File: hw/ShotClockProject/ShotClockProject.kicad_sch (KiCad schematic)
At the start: 5 parts, among them SW5 SW_SPDT

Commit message: Renamed references
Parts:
- renumbered R8 to R1, R12 to R2, SW5 to SW1, TP8 to TP2
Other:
- note added: "SPDT here is the main power switch. The TP4056 should still be able to run, when the product is turned off (to charge Li-Po). The TP4056 gets powered directly from 5V Vbus (USB-c cable)."
- note removed: "SW5 is the main power switch. The TP4056 should still be able to run, when the product is turned off (to charge Li-Po). The TP4056 gets powered directly from 5V Vbus (USB-c cable)."
- moved on the sheet: R2, TP2
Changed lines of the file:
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@@
   (junction (at 59.69 49.53) (diameter 0) (color 0 0 0 0)
   )
-  (junction (at 149.86 48.26) (diameter 0) (color 0 0 0 0)
-  )
-  (junction (at 138.43 48.26) (diameter 0) (color 0 0 0 0)
+  (junction (at 149.86 50.8) (diameter 0) (color 0 0 0 0)
+  )
+  (junction (at 138.43 50.8) (diameter 0) (color 0 0 0 0)
   )
   (no_connect (at 81.28 46.99))
@@
     (stroke (width 0) (type default))
   )
-  (wire (pts (xy 138.43 48.26) (xy 139.7 48.26))
+  (wire (pts (xy 138.43 50.8) (xy 139.7 50.8))
     (stroke (width 0) (type default))
   )
@@
     (stroke (width 0) (type default))
   )
-  (wire (pts (xy 90.17 48.26) (xy 101.6 48.26))
+  (wire (pts (xy 90.17 50.8) (xy 90.17 52.07))
     (stroke (width 0) (type default))
   )
@@
     (stroke (width 0) (type default))
   )
-  (wire (pts (xy 125.73 48.26) (xy 138.43 48.26))
+  (wire (pts (xy 125.73 50.8) (xy 138.43 50.8))
     (stroke (width 0) (type default))
   )
@@
     (stroke (width 0) (type default))
   )
-  (wire (pts (xy 153.67 48.26) (xy 153.67 46.99))
+  (wire (pts (xy 153.67 50.8) (xy 153.67 49.53))
     (stroke (width 0) (type default))
   )
@@
     (stroke (width 0) (type default))
   )
-  (wire (pts (xy 147.32 48.26) (xy 149.86 48.26))
+  (wire (pts (xy 147.32 50.8) (xy 149.86 50.8))
     (stroke (width 0) (type default))
   )
@@
     (stroke (width 0) (type default))
   )
-  (wire (pts (xy 90.17 52.07) (xy 90.17 48.26))
-    (stroke (width 0) (type default))
-  )
   (wire (pts (xy 203.2 78.74) (xy 231.14 78.74))
     (stroke (width 0) (type default))
   )
-  (wire (pts (xy 149.86 48.26) (xy 153.67 48.26))
+  (wire (pts (xy 149.86 50.8) (xy 153.67 50.8))
+    (stroke (width 0) (type default))
+  )
+  (wire (pts (xy 101.6 50.8) (xy 90.17 50.8))
     (stroke (width 0) (type default))
   )
@@
     (effects (font (size 2.5 2.5) (color 255 0 0 1)) (justify left bottom))
   )
-  (text "SW5 is the main power switch.\nThe TP4056 should still be able to run, \nwhen the product is turned off (to charge Li-Po).\nThe TP4056 gets powered directly from 5V Vbus (USB-c cable)."
+  (text "SPDT here is the main power switch.\nThe TP4056 should still be able to run, \nwhen the product is turned off (to charge Li-Po).\nThe TP4056 gets powered directly from 5V Vbus (USB-c cable)."
     (at 46.99 83.82 0)
     (effects (font (size 1.27 1.27)) (justify left bottom))
@@
   (symbol (lib_id "Switch:SW_SPDT") (at 76.2 49.53 0) (unit 1)
     (in_bom yes) (on_board yes) (dnp no)
-    (property "Reference" "SW5" (at 73.66 52.07 0)
+    (property "Reference" "SW1" (at 73.66 52.07 0)
       (effects (font (size 1.27 1.27)))
     )
@@
       (project "ShotClockProject"
         (path "/5fd859aa-754d-49c2-9762-3f7ebe3bb64c"
-          (reference "SW5") (unit 1)
+          (reference "SW1") (unit 1)
         )
         (path "/5fd859aa-754d-49c2-9762-3f7ebe3bb64c/d53b1cd8-24cb-4dc0-9a02-0cd96c1f4291"
@@
   (symbol (lib_id "Device:R") (at 64.77 49.53 90) (unit 1)
     (in_bom yes) (on_board yes) (dnp no) (fields_autoplaced)
-    (property "Reference" "R8" (at 64.77 43.18 90)
+    (property "Reference" "R1" (at 64.77 43.18 90)
       (effects (font (size 1.27 1.27)))
     )
@@
       (project "ShotClockProject"
         (path "/5fd859aa-754d-49c2-9762-3f7ebe3bb64c"
-          (reference "R8") (unit 1)
-        )
-      )
-    )
-  )
-  (symbol (lib_id "Connector:TestPoint") (at 138.43 48.26 0) (mirror y) (unit 1)
+          (reference "R1") (unit 1)
+        )
+      )
+    )
+  )
+  (symbol (lib_id "Connector:TestPoint") (at 138.43 50.8 0) (mirror y) (unit 1)
     (in_bom yes) (on_board yes) (dnp no)
-    (property "Reference" "TP8" (at 137.16 43.18 0)
-      (effects (font (size 1.27 1.27)) (justify left))
-    )
-    (property "Value" "TestPoint" (at 137.16 45.72 0)
-      (effects (font (size 1.27 1.27)) (justify left))
-    )
-    (property "Footprint" "TestPoint:TestPoint_Pad_D2.5mm" (at 133.35 48.26 0)
-      (effects (font (size 1.27 1.27)) hide)
-    )
-    (property "Datasheet" "~" (at 133.35 48.26 0)
-      (effects (font (size 1.27 1.27)) hide)
-    )
-    (pin "1")
-    (instances
-      (project "ShotClockProject"
-        (path "/5fd859aa-754d-49c2-9762-3f7ebe3bb64c"
-          (reference "TP8") (unit 1)
+    (property "Reference" "TP2" (at 137.16 45.72 0)
+      (effects (font (size 1.27 1.27)) (justify left))
+    )
+    (property "Value" "TestPoint" (at 137.16 48.26 0)
+      (effects (font (size 1.27 1.27)) (justify left))
+    )
+    (property "Footprint" "TestPoint:TestPoint_Pad_D2.5mm" (at 133.35 50.8 0)
+      (effects (font (size 1.27 1.27)) hide)
+    )
+    (property "Datasheet" "~" (at 133.35 50.8 0)
+      (effects (font (size 1.27 1.27)) hide)
+    )
+    (pin "1")
+    (instances
+      (project "ShotClockProject"
+        (path "/5fd859aa-754d-49c2-9762-3f7ebe3bb64c"
+          (reference "TP2") (unit 1)
         )
         (path "/5fd859aa-754d-49c2-9762-3f7ebe3bb64c/17367eb9-0f4d-4017-b1ca-d50430410a5d"
@@
     )
   )
-  (symbol (lib_id "Device:R") (at 143.51 48.26 90) (unit 1)
+  (symbol (lib_id "Device:R") (at 143.51 50.8 90) (unit 1)
     (in_bom yes) (on_board yes) (dnp no) (fields_autoplaced)
-    (property "Reference" "R12" (at 143.51 41.91 90)
-      (effects (font (size 1.27 1.27)))
-    )
-    (property "Value" "0R" (at 143.51 44.45 90)
-      (effects (font (size 1.27 1.27)))
-    )
-    (property "Footprint" "Resistor_SMD:R_0603_1608Metric" (at 143.51 50.038 90)
-      (effects (font (size 1.27 1.27)) hide)
-    )
-    (property "Datasheet" "~" (at 143.51 48.26 0)
+    (property "Reference" "R2" (at 143.51 44.45 90)
+      (effects (font (size 1.27 1.27)))
+    )
+    (property "Value" "0R" (at 143.51 46.99 90)
+      (effects (font (size 1.27 1.27)))
+    )
+    (property "Footprint" "Resistor_SMD:R_0603_1608Metric" (at 143.51 52.578 90)
+      (effects (font (size 1.27 1.27)) hide)
+    )
+    (property "Datasheet" "~" (at 143.51 50.8 0)
       (effects (font (size 1.27 1.27)) hide)
     )
@@
       (project "ShotClockProject"
         (path "/5fd859aa-754d-49c2-9762-3f7ebe3bb64c"
-          (reference "R12") (unit 1)
-        )
-      )
-    )
-  )
-  (symbol (lib_id "power:PWR_FLAG") (at 149.86 48.26 180) (unit 1)
+          (reference "R2") (unit 1)
+        )
+      )
+    )
+  )
+  (symbol (lib_id "power:PWR_FLAG") (at 149.86 50.8 180) (unit 1)
     (in_bom yes) (on_board yes) (dnp no) (fields_autoplaced)
-    (property "Reference" "#FLG02" (at 149.86 50.165 0)
-      (effects (font (size 1.27 1.27)) hide)
-    )
-    (property "Value" "PWR_FLAG" (at 149.86 53.34 0)
-      (effects (font (size 1.27 1.27)))
-    )
-    (property "Footprint" "" (at 149.86 48.26 0)
-      (effects (font (size 1.27 1.27)) hide)
-    )
-    (property "Datasheet" "~" (at 149.86 48.26 0)
+    (property "Reference" "#FLG02" (at 149.86 52.705 0)
+      (effects (font (size 1.27 1.27)) hide)
+    )
+    (property "Value" "PWR_FLAG" (at 149.86 55.88 0)
+      (effects (font (size 1.27 1.27)))
+    )
+    (property "Footprint" "" (at 149.86 50.8 0)
+      (effects (font (size 1.27 1.27)) hide)
+    )
+    (property "Datasheet" "~" (at 149.86 50.8 0)
       (effects (font (size 1.27 1.27)) hide)
     )
@@
         )
         (path "/5fd859aa-754d-49c2-9762-3f7ebe3bb64c"
-          (reference "#FLG03") (unit 1)
-        )
-      )
-    )
-  )
-  (symbol (lib_id "power:+3.3V") (at 153.67 46.99 0) (unit 1)
+          (reference "#FLG01") (unit 1)
+        )
+      )
+    )
+  )
+  (symbol (lib_id "power:+3.3V") (at 153.67 49.53 0) (unit 1)
     (in_bom yes) (on_board yes) (dnp no)
-    (property "Reference" "#PWR033" (at 153.67 50.8 0)
-      (effects (font (size 1.27 1.27)) hide)
-    )
-    (property "Value" "+3.3V" (at 153.67 43.18 0)
-      (effects (font (size 1.27 1.27)))
-    )
-    (property "Footprint" "" (at 153.67 46.99 0)
-      (effects (font (size 1.27 1.27)) hide)
-    )
-    (property "Datasheet" "" (at 153.67 46.99 0)
-      (effects (font (size 1.27 1.27)) hide)
-    )
-    (pin "1")
-    (instances
-      (project "ShotClockProject"
-        (path "/5fd859aa-754d-49c2-9762-3f7ebe3bb64c"
-          (reference "#PWR033") (unit 1)
+    (property "Reference" "#PWR01" (at 153.67 53.34 0)
+      (effects (font (size 1.27 1.27)) hide)
+    )
+    (property "Value" "+3.3V" (at 153.67 45.72 0)
+      (effects (font (size 1.27 1.27)))
+    )
+    (property "Footprint" "" (at 153.67 49.53 0)
+      (effects (font (size 1.27 1.27)) hide)
+    )
+    (property "Datasheet" "" (at 153.67 49.53 0)
+      (effects (font (size 1.27 1.27)) hide)
+    )
+    (pin "1")
+    (instances
+      (project "ShotClockProject"
+        (path "/5fd859aa-754d-49c2-9762-3f7ebe3bb64c"
+          (reference "#PWR01") (unit 1)
         )
         (path "/5fd859aa-754d-49c2-9762-3f7ebe3bb64c/d53b1cd8-24cb-4dc0-9a02-0cd96c1f4291"
@@
     )
   )
-  (sheet (at 101.6 39.37) (size 24.13 19.05) (fields_autoplaced)
+  (sheet (at 101.6 41.91) (size 24.13 19.05) (fields_autoplaced)
     (stroke (width 0.1524) (type solid))
     (fill (color 0 0 0 0.0000))
-    (property "Sheetname" "Voltage regulator 3v3" (at 101.6 38.6584 0)
+    (property "Sheetname" "Voltage regulator 3v3" (at 101.6 41.1984 0)
       (effects (font (size 1.27 1.27)) (justify left bottom))
     )
-    (property "Sheetfile" "Regulator3V3.kicad_sch" (at 101.6 59.0046 0)
+    (property "Sheetfile" "Regulator3V3.kicad_sch" (at 101.6 61.5446 0)
       (effects (font (size 1.27 1.27)) (justify left top))
     )
-    (pin "batt_in" input (at 101.6 48.26 180)
-      (effects (font (size 1.27 1.27)) (justify left))
-    )
-    (pin "3v3_out" output (at 125.73 48.26 0)
+    (pin "batt_in" input (at 101.6 50.8 180)
+      (effects (font (size 1.27 1.27)) (justify left))
+    )
+    (pin "3v3_out" output (at 125.73 50.8 0)
       (effects (font (size 1.27 1.27)) (justify right))
     )

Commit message: Changed footprint
To horizontal 2.54 connectors
and started on rough layout
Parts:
- R1, R2: footprint Resistor_SMD:R_0603_1608Metric -> Resistor_SMD:R_0402_1005Metric
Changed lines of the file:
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@@
       (effects (font (size 1.27 1.27)))
     )
-    (property "Footprint" "Resistor_SMD:R_0603_1608Metric" (at 64.77 51.308 90)
+    (property "Footprint" "Resistor_SMD:R_0402_1005Metric" (at 64.77 51.308 90)
       (effects (font (size 1.27 1.27)) hide)
     )
@@
       (effects (font (size 1.27 1.27)))
     )
-    (property "Footprint" "Resistor_SMD:R_0603_1608Metric" (at 143.51 52.578 90)
+    (property "Footprint" "Resistor_SMD:R_0402_1005Metric" (at 143.51 52.578 90)
       (effects (font (size 1.27 1.27)) hide)
     )

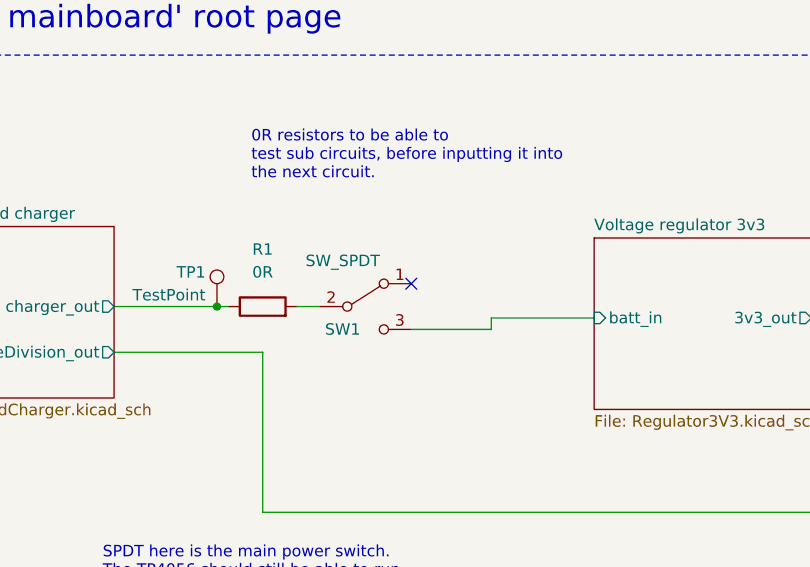
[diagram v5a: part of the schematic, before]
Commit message: Finished rough layout of PCB (ready for review)
Changed battery polarity to match the batteries I have.
Added power led to voltage regulator
Removed old comments from schematic
Gave all footprints a 3D model
Replaced batttery footprint with a SMD JST 3 pins horizontal connector
Finished rough placement of components
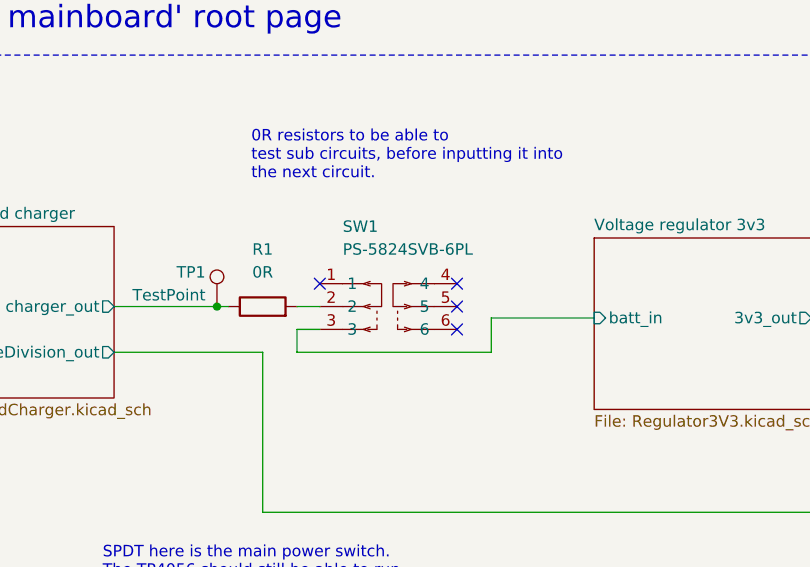
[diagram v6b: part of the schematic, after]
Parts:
- removed SW1: SW_SPDT, Button_Switch_SMD:SW_SPDT_PCM12, symbol Switch:SW_SPDT
- added SW1: PS-5824SVB-6PL, PS-5824SVB-6PL:SW-SMD_6P-L5.8-W5.8-P2.00-LS11.3, symbol PS-5824SVB-6PL:PS-5824SVB-6PL
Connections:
- net Voltage regulator 3v3/batt_in: now also SW1.3
- net at R1.2: now also SW1.2
- no-connect marks 1 -> 4
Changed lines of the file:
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@@
   (junction (at 138.43 50.8) (diameter 0) (color 0 0 0 0)
   )
-  (no_connect (at 81.28 46.99))
+  (no_connect (at 86.36 52.07))
+  (no_connect (at 86.36 49.53))
+  (no_connect (at 86.36 46.99))
+  (no_connect (at 71.12 46.99))
   (wire (pts (xy 203.2 50.8) (xy 231.14 50.8))
     (stroke (width 0) (type default))
@@
     (stroke (width 0) (type default))
   )
-  (wire (pts (xy 90.17 50.8) (xy 90.17 52.07))
+  (wire (pts (xy 90.17 50.8) (xy 90.17 54.61))
+    (stroke (width 0) (type default))
+  )
+  (wire (pts (xy 68.58 54.61) (xy 68.58 52.07))
     (stroke (width 0) (type default))
   )
@@
     (stroke (width 0) (type default))
   )
+  (wire (pts (xy 90.17 54.61) (xy 68.58 54.61))
+    (stroke (width 0) (type default))
+  )
   (wire (pts (xy 59.69 49.53) (xy 60.96 49.53))
     (stroke (width 0) (type default))
@@
     (stroke (width 0) (type default))
   )
+  (wire (pts (xy 68.58 52.07) (xy 71.12 52.07))
+    (stroke (width 0) (type default))
+  )
   (wire (pts (xy 149.86 50.8) (xy 153.67 50.8))
     (stroke (width 0) (type default))
@@
   )
   (wire (pts (xy 203.2 90.17) (xy 231.14 90.17))
-    (stroke (width 0) (type default))
-  )
-  (wire (pts (xy 81.28 52.07) (xy 90.17 52.07))
     (stroke (width 0) (type default))
   )
@@
     (effects (font (size 1.27 1.27)) (justify left bottom))
   )
-  (symbol (lib_id "Switch:SW_SPDT") (at 76.2 49.53 0) (unit 1)
-    (in_bom yes) (on_board yes) (dnp no)
-    (property "Reference" "SW1" (at 73.66 52.07 0)
-      (effects (font (size 1.27 1.27)))
-    )
-    (property "Value" "SW_SPDT" (at 73.66 44.45 0)
-      (effects (font (size 1.27 1.27)))
-    )
-    (property "Footprint" "Button_Switch_SMD:SW_SPDT_PCM12" (at 76.2 49.53 0)
-      (effects (font (size 1.27 1.27)) hide)
-    )
-    (property "Datasheet" "~" (at 76.2 49.53 0)
-      (effects (font (size 1.27 1.27)) hide)
-    )
-    (pin "1")
-    (pin "2")
-    (pin "3")
-    (instances
-      (project "ShotClockProject"
-        (path "/5fd859aa-754d-49c2-9762-3f7ebe3bb64c"
-          (reference "SW1") (unit 1)
-        )
-        (path "/5fd859aa-754d-49c2-9762-3f7ebe3bb64c/d53b1cd8-24cb-4dc0-9a02-0cd96c1f4291"
-          (reference "SW1") (unit 1)
-        )
-      )
-    )
-  )
   (symbol (lib_id "Device:R") (at 64.77 49.53 90) (unit 1)
     (in_bom yes) (on_board yes) (dnp no) (fields_autoplaced)
@@
         )
       )
+    )
+  )
+  (symbol (lib_id "PS-5824SVB-6PL:PS-5824SVB-6PL") (at 78.74 49.53 270) (unit 1)
+    (in_bom yes) (on_board yes) (dnp no)
+    (property "Reference" "SW1" (at 73.66 40.64 90)
+      (effects (font (size 1.27 1.27)) (justify left))
+    )
+    (property "Value" "PS-5824SVB-6PL" (at 73.66 43.18 90)
+      (effects (font (size 1.27 1.27)) (justify left))
+    )
+    (property "Footprint" "PS-5824SVB-6PL:SW-SMD_6P-L5.8-W5.8-P2.00-LS11.3" (at 63.5 49.53 0)
+      (effects (font (size 1.27 1.27)) hide)
+    )
+    (property "Datasheet" "" (at 78.74 49.53 0)
+      (effects (font (size 1.27 1.27)) hide)
+    )
+    (property "Manufacturer" "G-Switch(品赞)" (at 60.96 49.53 0)
+      (effects (font (size 1.27 1.27)) hide)
+    )
+    (property "LCSC Part" "C5155575" (at 58.42 49.53 0)
+      (effects (font (size 1.27 1.27)) hide)
+    )
+    (pin "1")
+    (pin "2")
+    (pin "3")
+    (pin "4")
+    (pin "5")
+    (pin "6")
+    (instances
+      (project "ShotClockProject"
+        (path "/5fd859aa-754d-49c2-9762-3f7ebe3bb64c"
+          (reference "SW1") (unit 1)
+        )
+      )

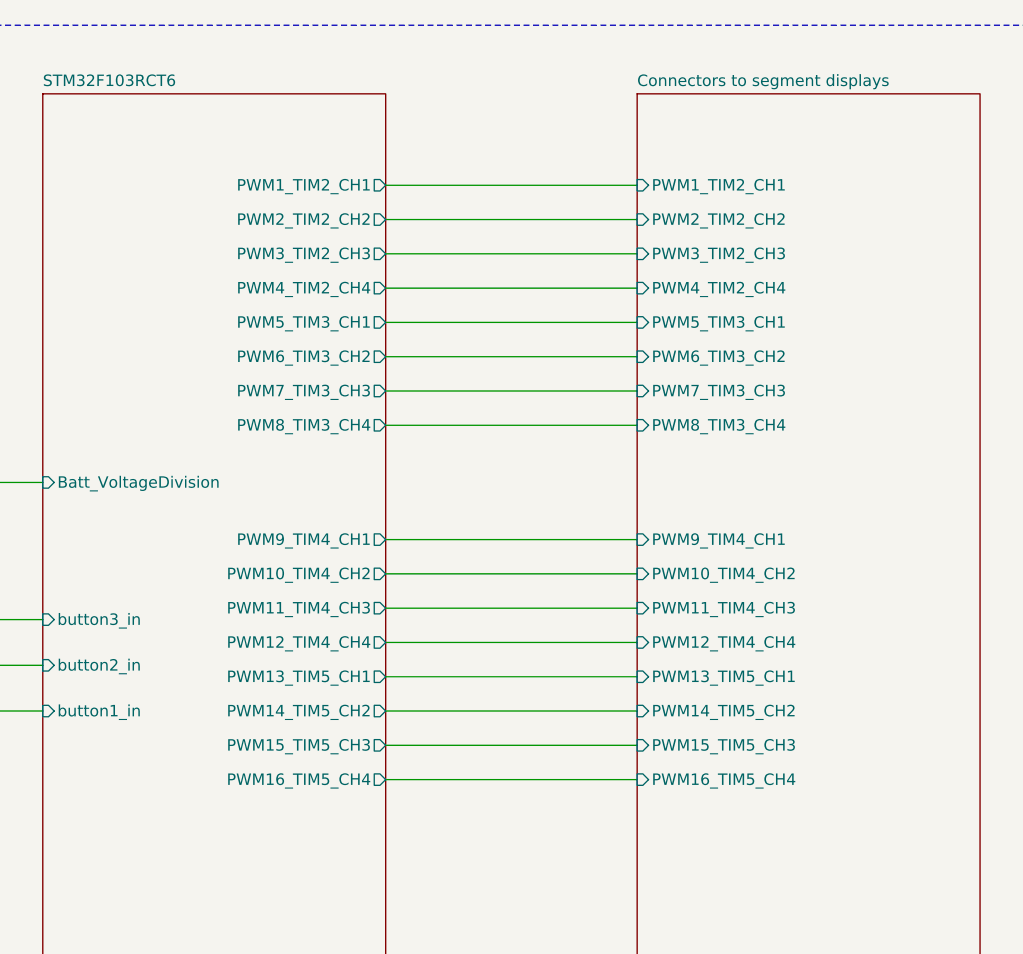
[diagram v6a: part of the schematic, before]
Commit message: Changed pinouts
To only use 1 pwm per display, and GPIo outs for the rest in both HW and firmware
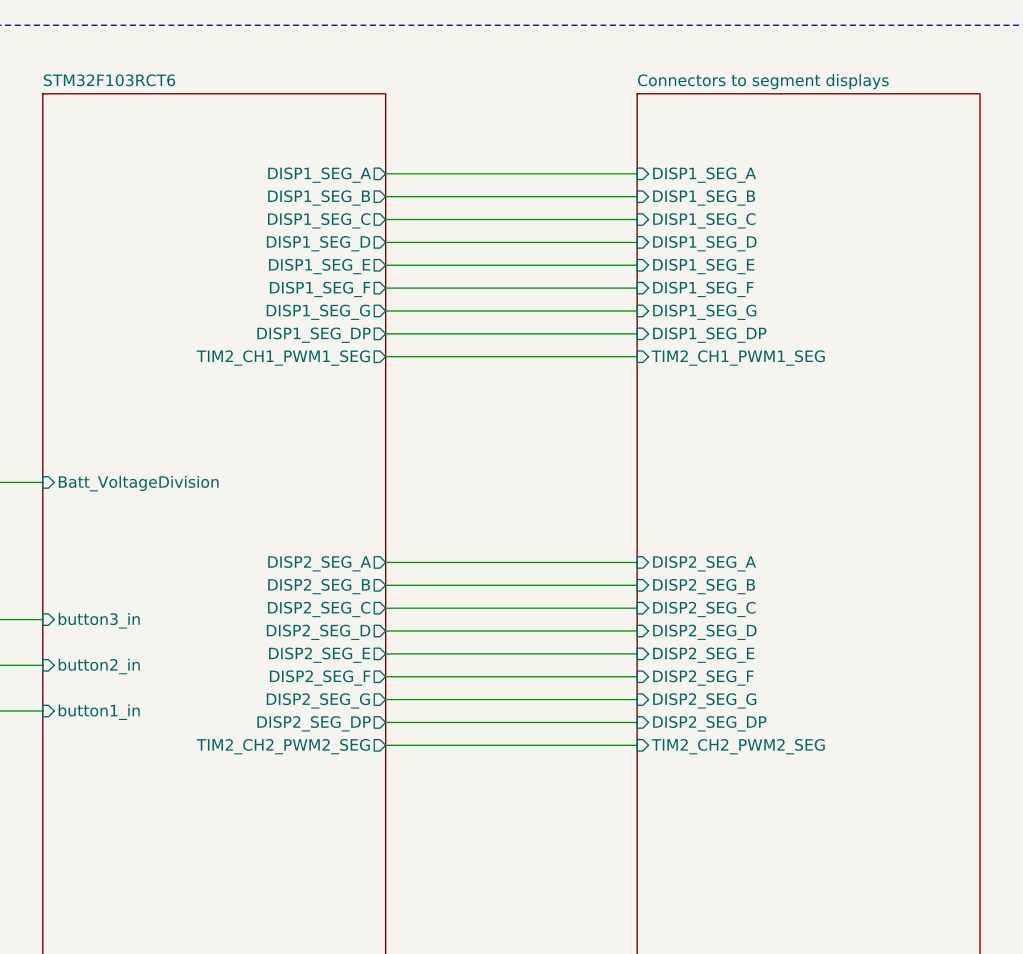
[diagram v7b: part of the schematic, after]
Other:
- sheet Connectors to segment displays ports: added DISP1_SEG_A, DISP1_SEG_B, DISP1_SEG_C, DISP1_SEG_D, DISP1_SEG_DP, DISP1_SEG_E, DISP1_SEG_F, DISP1_SEG_G, DISP2_SEG_A, DISP2_SEG_B, DISP2_SEG_C, DISP2_SEG_D, DISP2_SEG_DP, DISP2_SEG_E, DISP2_SEG_F, DISP2_SEG_G, TIM2_CH1_PWM1_SEG, TIM2_CH2_PWM2_SEG; removed PWM10_TIM4_CH2, PWM11_TIM4_CH3, PWM12_TIM4_CH4, PWM13_TIM5_CH1, PWM14_TIM5_CH2, PWM15_TIM5_CH3, PWM16_TIM5_CH4, PWM1_TIM2_CH1, PWM2_TIM2_CH2, PWM3_TIM2_CH3, PWM4_TIM2_CH4, PWM5_TIM3_CH1, PWM6_TIM3_CH2, PWM7_TIM3_CH3, PWM8_TIM3_CH4, PWM9_TIM4_CH1
- sheet STM32F103RCT6 ports: added DISP1_SEG_A, DISP1_SEG_B, DISP1_SEG_C, DISP1_SEG_D, DISP1_SEG_DP, DISP1_SEG_E, DISP1_SEG_F, DISP1_SEG_G, DISP2_SEG_A, DISP2_SEG_B, DISP2_SEG_C, DISP2_SEG_D, DISP2_SEG_DP, DISP2_SEG_E, DISP2_SEG_F, DISP2_SEG_G, TIM2_CH1_PWM1_SEG, TIM2_CH2_PWM2_SEG; removed PWM10_TIM4_CH2, PWM11_TIM4_CH3, PWM12_TIM4_CH4, PWM13_TIM5_CH1, PWM14_TIM5_CH2, PWM15_TIM5_CH3, PWM16_TIM5_CH4, PWM1_TIM2_CH1, PWM2_TIM2_CH2, PWM3_TIM2_CH3, PWM4_TIM2_CH4, PWM5_TIM3_CH1, PWM6_TIM3_CH2, PWM7_TIM3_CH3, PWM8_TIM3_CH4, PWM9_TIM4_CH1
